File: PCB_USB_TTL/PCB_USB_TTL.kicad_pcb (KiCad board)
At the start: 2 copper layers, 22 x 36 mm, 27 parts, among them J1 Conn_01x03_Male, J2 Conn_01x06_Male, J3 Conn_01x02_Male, J4 Conn_01x02_Male, P1 USB_C_Plug, Q1 BC817, Q2 BC817, U1 AZ1117H-3.3TRE1, U2 CH340G

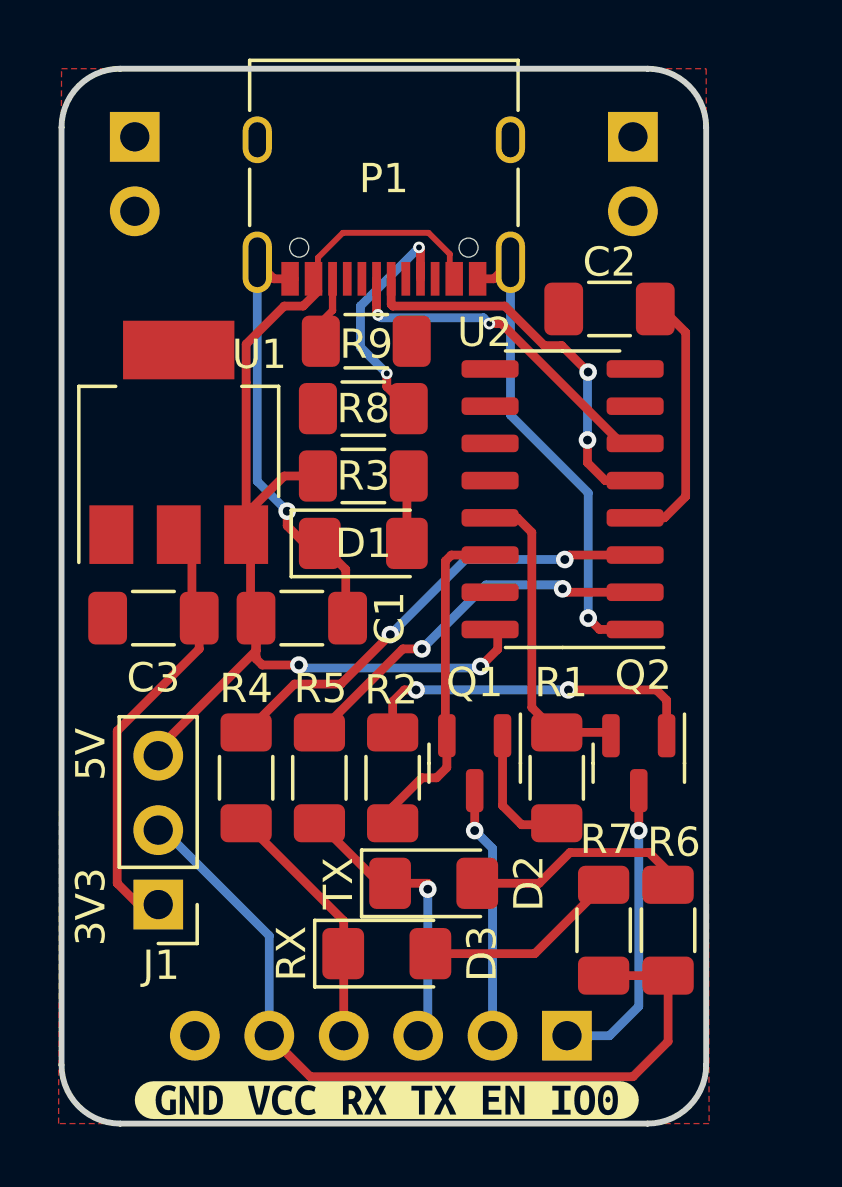
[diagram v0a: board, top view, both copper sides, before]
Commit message: Rev 2
Switch is added to change from 3.3v to 5v.

UMH3N is used to save space and cost.
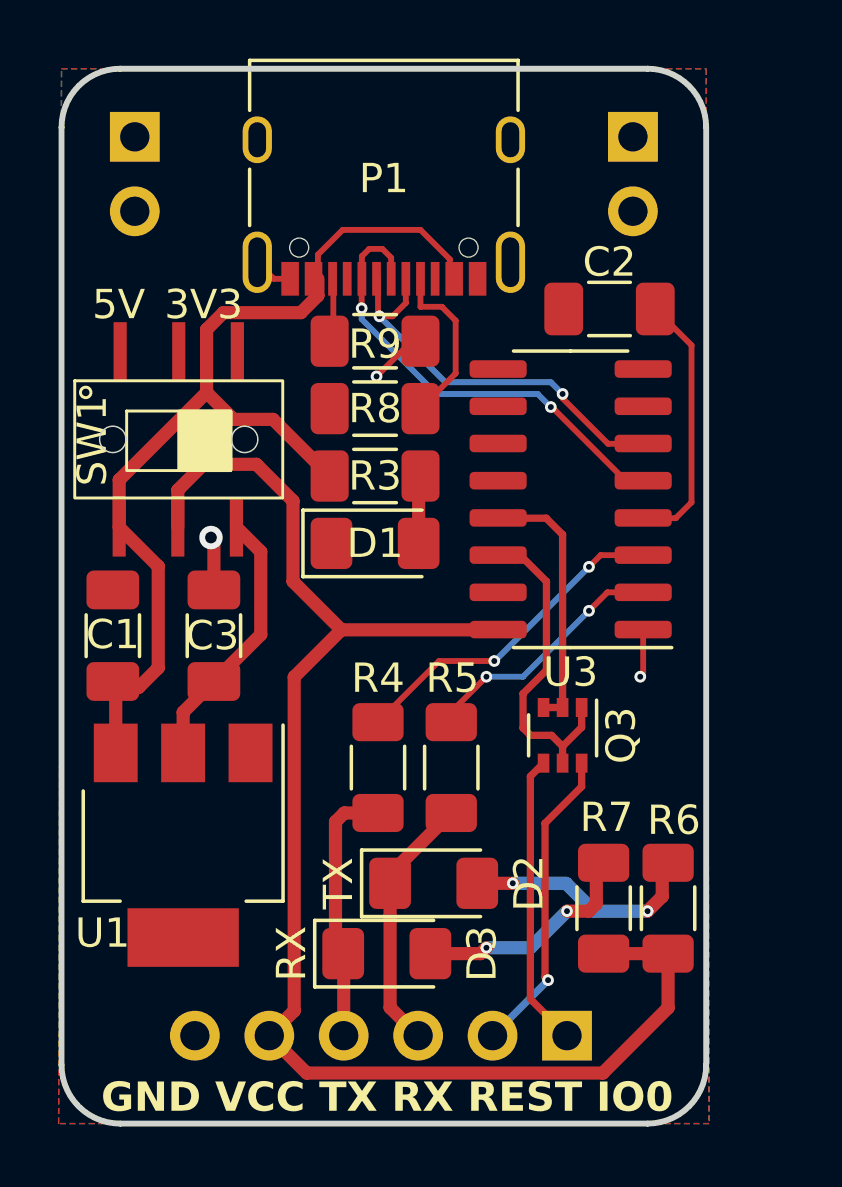
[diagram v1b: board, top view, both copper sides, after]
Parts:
- removed J1: Conn_01x03_Male, Connector_PinHeader_2.54mm:PinHeader_1x03_P2.54mm_Vertical
- removed Q1, Q2: BC817, Package_TO_SOT_SMD:SOT-23
- removed R1, R2: 1K, Resistor_SMD:R_1206_3216Metric_Pad1.30x1.75mm_HandSolder
- removed U2: CH340G, Package_SO:SOIC-16_3.9x9.9mm_P1.27mm
- removed kibuzzard-638EC2B1: G***, kibuzzard-638EC2B1
- added Q3: UMH3N, Package_TO_SOT_SMD:SOT-363_SC-70-6, F.Cu at (149.6, 83.8)
- added SW1: ~, JAPS:MS-22D28-G020, F.Cu at (136.5, 70.7)
- added U3: CH340C, Package_SO:SOIC-16_3.9x9.9mm_P1.27mm, F.Cu at (149.9, 75.7)
- R3: value 220 -> 1K
- moved U1 13.8 mm to (136.7, 87.5), turned to -90 degrees
- moved C1 6.48 mm to (134.2, 80.3), turned to 90 degrees
- moved R4 4.51 mm to (145.8, 84.8)
- moved R5 4.51 mm to (143.3, 84.8)
- moved C3 2.15 mm to (137.7, 80.3), turned to 90 degrees
- moved R6 0.75 mm to (153.2, 89.7)
- moved R7 0.75 mm to (151.0, 89.7)
- moved D1 0.40 mm to (143.2, 77.2)
- moved R3 0.40 mm to (143.2, 74.9)
- moved R8 0.40 mm to (143.2, 72.6)
- moved R9 0.30 mm to (143.2, 70.3)
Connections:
- J2 pad 2: /ESP_EN -> /REST
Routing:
- net GND: track 31.4 -> 6.68 mm, vias 2 -> 3
- net VCC: track 27.8 -> 50.2 mm
- net Net-(Q2-Pad1): track 11.9 -> 0.00 mm, vias 2 -> 0
- net /REST: track 0.00 -> 10.6 mm, vias 0 -> 1
- net /ESP_EN: track 8.62 -> 0.00 mm, vias 1 -> 0
- net +3.3V: track 15.0 -> 9.14 mm
- net +5V: track 40.3 -> 34.4 mm, vias 2 -> 0
- net Net-(Q1-Pad1): track 4.53 -> 0.00 mm
- net Net-(U3-TXD): track 13.0 -> 8.59 mm
- net Net-(U3-RXD): track 15.8 -> 11.4 mm
- net Net-(P1-CC): track 8.10 -> 5.85 mm, vias 2 -> 0
- net /D+: track 13.8 -> 15.7 mm
- net /D-: track 12.1 -> 13.9 mm
- net /DTR: track 10.4 -> 9.23 mm
- net /TX: track 9.89 -> 8.86 mm, vias 1 -> 0
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- added copper zone on B.Cu, net GND
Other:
- board text added: "GND VCC TX RX REST IO0"
